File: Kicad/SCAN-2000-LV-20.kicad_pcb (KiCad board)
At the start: 2 copper layers, 220 x 67 mm, 151 parts, among them J1 FTDI, J10 OUTPUT-BUS-A, J11 OUTPUT-BUS-B, J12 Test, J13 Conn_02x04_Counter_Clockwise, J2 Conn_01x02, J3 Conn_01x02, J4 BUS-A-INPUT, J5 SWD, J6 BUS-A-INPUT, J7 BUS-B-INPUT, J8 BUS-B-INPUT, J9 MOLEX 85050-0000, K1 EC2-3TNU, U1 STM32G030, U10 DG412, U11 DG412, U12 RB-0515D, U13 MDC3105, U14 TPS78233DDC, U15 TL7733BD, U16 MDC3105, U17 RB-0505S, U2 DG412, U3 DG412, U4 DG412, U5 DG412, U6 DG412, U7 DG412, U8 DG412, U9 DG412

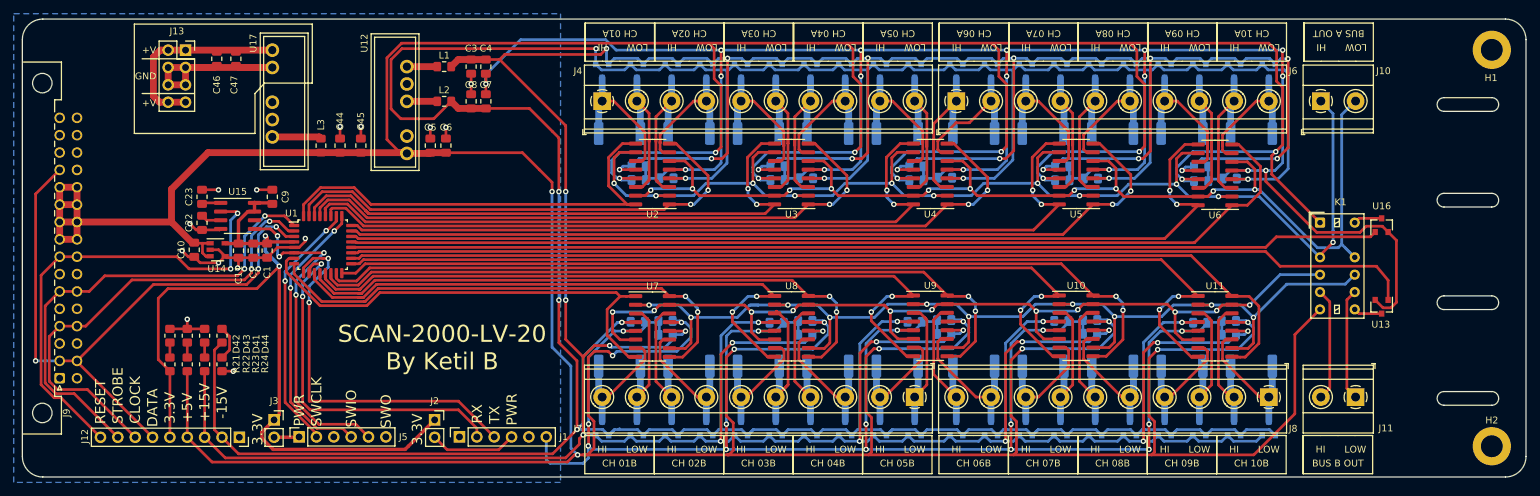
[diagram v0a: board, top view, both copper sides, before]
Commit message: Board layout for the Switches
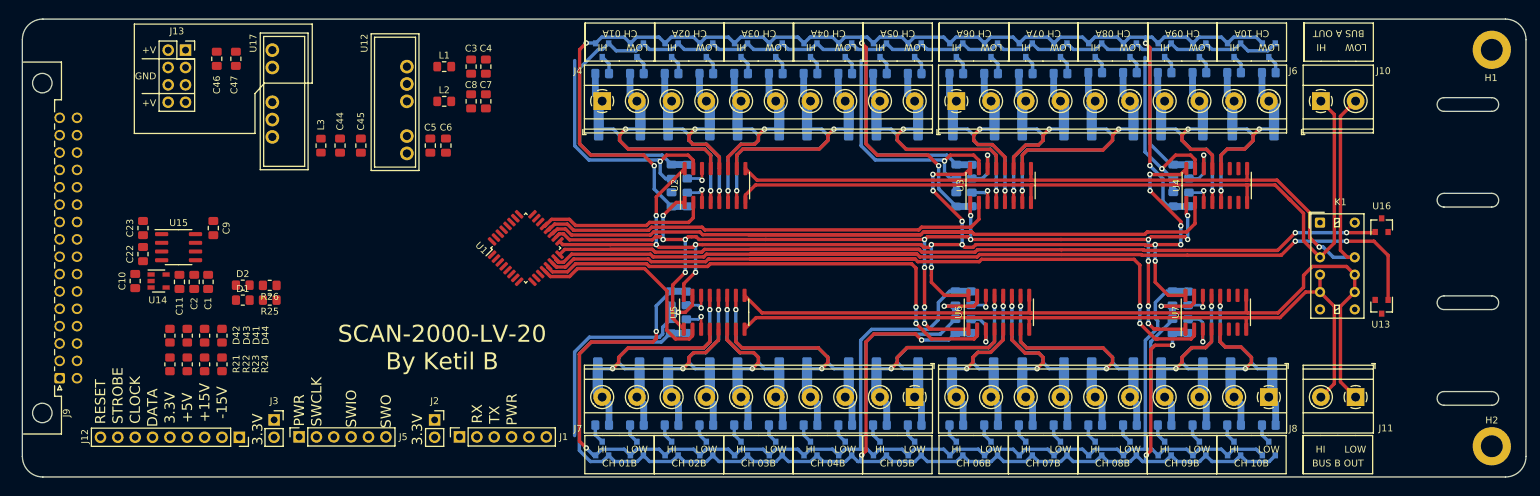
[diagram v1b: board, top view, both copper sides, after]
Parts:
- removed C13, C15, C17, C18, C19, C20, C21, C25, C27, C30, C32, C34, C35, C36, C37, C38, C40, C42: 0.1u, Capacitors-SMD:C_0805_2012Metric_Pad1.18x1.45mm_HandSolder
- removed U10, U11, U8, U9: DG412, SMD-SO:SOIC-16_3.9x9.9mm_P1.27mm
- added D45: BAV199, Package_TO_SOT_SMD:SOT-23, B.Cu at (185.3, 629.3)
- added D46: BAV199, Package_TO_SOT_SMD:SOT-23, B.Cu at (190.4, 629.3)
- added D47: BAV199, Package_TO_SOT_SMD:SOT-23, B.Cu at (195.5, 629.3)
- added D48: BAV199, Package_TO_SOT_SMD:SOT-23, B.Cu at (200.6, 629.3)
- added D49: BAV199, Package_TO_SOT_SMD:SOT-23, B.Cu at (206.7, 629.3)
- added D50: BAV199, Package_TO_SOT_SMD:SOT-23, B.Cu at (211.7, 629.3)
- added D51: BAV199, Package_TO_SOT_SMD:SOT-23, B.Cu at (216.8, 629.3)
- added D52: BAV199, Package_TO_SOT_SMD:SOT-23, B.Cu at (221.9, 629.3)
- added D53: BAV199, Package_TO_SOT_SMD:SOT-23, B.Cu at (227.0, 629.3)
- added D54: BAV199, Package_TO_SOT_SMD:SOT-23, B.Cu at (232.1, 629.3)
- added D55: BAV199, Package_TO_SOT_SMD:SOT-23, B.Cu at (237.1, 629.3)
- added D56: BAV199, Package_TO_SOT_SMD:SOT-23, B.Cu at (242.2, 629.3)
- added D57: BAV199, Package_TO_SOT_SMD:SOT-23, B.Cu at (247.3, 629.3)
- added D58: BAV199, Package_TO_SOT_SMD:SOT-23, B.Cu at (252.4, 629.3)
- added R100: 200R, Resistors-SMD:R_0805_2012Metric_Pad1.20x1.40mm_HandSolder, B.Cu at (221.9, 625.9)
- added R101: 200R, Resistors-SMD:R_0805_2012Metric_Pad1.20x1.40mm_HandSolder, B.Cu at (227.0, 625.9)
- added R102: 200R, Resistors-SMD:R_0805_2012Metric_Pad1.20x1.40mm_HandSolder, B.Cu at (232.1, 625.9)
- added R103: 200R, Resistors-SMD:R_0805_2012Metric_Pad1.20x1.40mm_HandSolder, B.Cu at (237.1, 625.9)
- added R104: 200R, Resistors-SMD:R_0805_2012Metric_Pad1.20x1.40mm_HandSolder, B.Cu at (242.2, 625.9)
- added R105: 200R, Resistors-SMD:R_0805_2012Metric_Pad1.20x1.40mm_HandSolder, B.Cu at (247.3, 625.9)
- added R106: 200R, Resistors-SMD:R_0805_2012Metric_Pad1.20x1.40mm_HandSolder, B.Cu at (252.4, 625.9)
- added R25: R, Resistors-SMD:R_0805_2012Metric_Pad1.20x1.40mm_HandSolder, F.Cu at (106.2, 607.6)
- added R26: R, Resistors-SMD:R_0805_2012Metric_Pad1.20x1.40mm_HandSolder, F.Cu at (106.2, 605.5)
- added R67: 200R, Resistors-SMD:R_0805_2012Metric_Pad1.20x1.40mm_HandSolder, B.Cu at (154.8, 574.5)
- added R68: 200R, Resistors-SMD:R_0805_2012Metric_Pad1.20x1.40mm_HandSolder, B.Cu at (159.9, 574.5)
- added R69: 200R, Resistors-SMD:R_0805_2012Metric_Pad1.20x1.40mm_HandSolder, B.Cu at (165.0, 574.5)
- added R70: 200R, Resistors-SMD:R_0805_2012Metric_Pad1.20x1.40mm_HandSolder, B.Cu at (170.1, 574.5)
- added R71: 200R, Resistors-SMD:R_0805_2012Metric_Pad1.20x1.40mm_HandSolder, B.Cu at (175.2, 574.5)
- added R72: 200R, Resistors-SMD:R_0805_2012Metric_Pad1.20x1.40mm_HandSolder, B.Cu at (180.2, 574.5)
- added R73: 200R, Resistors-SMD:R_0805_2012Metric_Pad1.20x1.40mm_HandSolder, B.Cu at (185.3, 574.5)
- added R74: 200R, Resistors-SMD:R_0805_2012Metric_Pad1.20x1.40mm_HandSolder, B.Cu at (190.4, 574.5)
- added R75: 200R, Resistors-SMD:R_0805_2012Metric_Pad1.20x1.40mm_HandSolder, B.Cu at (195.5, 574.5)
- added R76: 200R, Resistors-SMD:R_0805_2012Metric_Pad1.20x1.40mm_HandSolder, B.Cu at (200.6, 574.5)
- added R77: 200R, Resistors-SMD:R_0805_2012Metric_Pad1.20x1.40mm_HandSolder, B.Cu at (206.7, 574.5)
- added R78: 200R, Resistors-SMD:R_0805_2012Metric_Pad1.20x1.40mm_HandSolder, B.Cu at (211.7, 574.5)
- added R79: 200R, Resistors-SMD:R_0805_2012Metric_Pad1.20x1.40mm_HandSolder, B.Cu at (216.8, 574.5)
- added R80: 200R, Resistors-SMD:R_0805_2012Metric_Pad1.20x1.40mm_HandSolder, B.Cu at (221.9, 574.5)
- added R81: 200R, Resistors-SMD:R_0805_2012Metric_Pad1.20x1.40mm_HandSolder, B.Cu at (227.0, 574.3)
- added R82: 200R, Resistors-SMD:R_0805_2012Metric_Pad1.20x1.40mm_HandSolder, B.Cu at (232.1, 574.3)
- added R83: 200R, Resistors-SMD:R_0805_2012Metric_Pad1.20x1.40mm_HandSolder, B.Cu at (237.1, 574.3)
- added R84: 200R, Resistors-SMD:R_0805_2012Metric_Pad1.20x1.40mm_HandSolder, B.Cu at (242.2, 574.3)
- added R85: 200R, Resistors-SMD:R_0805_2012Metric_Pad1.20x1.40mm_HandSolder, B.Cu at (247.3, 574.3)
- added R86: 200R, Resistors-SMD:R_0805_2012Metric_Pad1.20x1.40mm_HandSolder, B.Cu at (252.4, 574.3)
- added R87: 200R, Resistors-SMD:R_0805_2012Metric_Pad1.20x1.40mm_HandSolder, B.Cu at (154.8, 625.9)
- added R88: 200R, Resistors-SMD:R_0805_2012Metric_Pad1.20x1.40mm_HandSolder, B.Cu at (159.9, 625.9)
- added R89: 200R, Resistors-SMD:R_0805_2012Metric_Pad1.20x1.40mm_HandSolder, B.Cu at (165.0, 625.9)
- added R90: 200R, Resistors-SMD:R_0805_2012Metric_Pad1.20x1.40mm_HandSolder, B.Cu at (170.1, 625.9)
- added R91: 200R, Resistors-SMD:R_0805_2012Metric_Pad1.20x1.40mm_HandSolder, B.Cu at (175.2, 625.9)
- added R92: 200R, Resistors-SMD:R_0805_2012Metric_Pad1.20x1.40mm_HandSolder, B.Cu at (180.2, 625.9)
- added R93: 200R, Resistors-SMD:R_0805_2012Metric_Pad1.20x1.40mm_HandSolder, B.Cu at (185.3, 625.9)
- added R94: 200R, Resistors-SMD:R_0805_2012Metric_Pad1.20x1.40mm_HandSolder, B.Cu at (190.4, 625.9)
- added R95: 200R, Resistors-SMD:R_0805_2012Metric_Pad1.20x1.40mm_HandSolder, B.Cu at (195.5, 625.9)
- added R96: 200R, Resistors-SMD:R_0805_2012Metric_Pad1.20x1.40mm_HandSolder, B.Cu at (200.6, 625.9)
- added R97: 200R, Resistors-SMD:R_0805_2012Metric_Pad1.20x1.40mm_HandSolder, B.Cu at (206.7, 625.9)
- added R98: 200R, Resistors-SMD:R_0805_2012Metric_Pad1.20x1.40mm_HandSolder, B.Cu at (211.7, 625.9)
- added R99: 200R, Resistors-SMD:R_0805_2012Metric_Pad1.20x1.40mm_HandSolder, B.Cu at (216.8, 625.9)
- D1, D2: value BAV199L -> LED; footprint SMD-SOT:SOT-23 -> Resistors-SMD:R_0805_2012Metric_Pad1.20x1.40mm_HandSolder; moved to F.Cu
- D10, D11, D12, D13, D14, D3, D4, D5, D6, D7, D8, D9: value BAV199L -> D; footprint SMD-SOT:SOT-23 -> Resistors-SMD:R_0805_2012Metric_Pad1.20x1.40mm_HandSolder
- D15, D16, D17, D18, D19, D20, D21, D22, D23, D24, D25, D26, D27, D28, D29, D30, D31, D32, D33, D34, D35, D36, D37, D38, D39, D40: value BAV199L -> BAV199; footprint SMD-SOT:SOT-23 -> Package_TO_SOT_SMD:SOT-23
- U2, U3, U4, U5, U6, U7: value DG412 -> DG409
- moved U7 82.4 mm to (244.6, 609.4), turned to 90 degrees
- moved D20 72.2 mm to (180.2, 571.0)
- moved D15 72.2 mm to (154.8, 571.0)
- moved D16 72.2 mm to (159.9, 571.0)
- moved D17 72.2 mm to (165.0, 571.0)
- moved D18 72.2 mm to (170.1, 571.0)
- moved D19 72.2 mm to (175.2, 571.0)
- moved D40 72.2 mm to (180.2, 629.3)
- moved D35 72.2 mm to (154.8, 629.3)
- moved D36 72.2 mm to (159.9, 629.3)
- moved D37 72.2 mm to (165.0, 629.3)
- moved D38 72.2 mm to (170.1, 629.3)
- moved D39 72.2 mm to (175.2, 629.3)
- moved D5 67.2 mm to (240.7, 588.8), turned to 90 degrees
- moved D2 65.6 mm to (102.2, 605.4), turned to 0 degrees
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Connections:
- D1 pad 1: -15V -> GND
- D1 pad 2: +15V -> Net-(D1-Pad2)
- D10 pad 1: -15V -> Net-(D10-Pad1)
- D11 pad 1: -15V -> Net-(D11-Pad1)
- D12 pad 2: +15V -> Net-(D12-Pad2)
- D13 pad 2: +15V -> Net-(D13-Pad2)
- D14 pad 2: +15V -> Net-(D14-Pad2)
- D15 pad 3: CHAN-08A-HI -> Net-(D15-Pad3)
- D16 pad 3: CHAN-08A-LO -> Net-(D16-Pad3)
- D17 pad 3: CHAN-09A-HI -> Net-(D17-Pad3)
- D18 pad 3: CHAN-09A-LO -> Net-(D18-Pad3)
- D19 pad 3: CHAN-10A-HI -> Net-(D19-Pad3)
- D2 pad 1: -15V -> GND
- D2 pad 2: +15V -> Net-(D2-Pad2)
- D20 pad 3: CHAN-10A-LO -> Net-(D20-Pad3)
- D21 pad 3: CHAN-01B-HI -> Net-(D21-Pad3)
- D22 pad 3: CHAN-01B-LO -> Net-(D22-Pad3)
- D23 pad 3: CHAN-02B-HI -> Net-(D23-Pad3)
- D24 pad 3: CHAN-02B-LO -> Net-(D24-Pad3)
- D25 pad 3: CHAN-03B-HI -> Net-(D25-Pad3)
- D26 pad 3: CHAN-03B-LO -> Net-(D26-Pad3)
- D27 pad 3: CHAN-04B-HI -> Net-(D27-Pad3)
- D28 pad 3: CHAN-04B-LO -> Net-(D28-Pad3)
- D29 pad 3: CHAN-05B-HI -> Net-(D29-Pad3)
- D3 pad 1: -15V -> Net-(D3-Pad1)
- D30 pad 3: CHAN-05B-LO -> Net-(D30-Pad3)
- D31 pad 3: CHAN-06B-HI -> Net-(D31-Pad3)
- D32 pad 3: CHAN-06B-LO -> Net-(D32-Pad3)
- D33 pad 3: CHAN-07B-HI -> Net-(D33-Pad3)
- D34 pad 3: CHAN-07B-LO -> Net-(D34-Pad3)
- D35 pad 3: CHAN-08B-HI -> Net-(D35-Pad3)
- D36 pad 3: CHAN-08B-LO -> Net-(D36-Pad3)
- D37 pad 3: CHAN-09B-HI -> Net-(D37-Pad3)
- D38 pad 3: CHAN-09B-LO -> Net-(D38-Pad3)
- D39 pad 3: CHAN-10B-HI -> Net-(D39-Pad3)
- D4 pad 1: -15V -> Net-(D4-Pad1)
- D40 pad 3: CHAN-10B-LO -> Net-(D40-Pad3)
- D5 pad 1: -15V -> Net-(D5-Pad1)
- D6 pad 2: +15V -> Net-(D6-Pad2)
- D7 pad 2: +15V -> Net-(D7-Pad2)
- D8 pad 2: +15V -> Net-(D8-Pad2)
- D9 pad 1: -15V -> Net-(D9-Pad1)
- J1 pad 1: DTR -> (no net)
- J1 pad 5: CTS -> (no net)
- J11 pad 1: Net-(J11-Pad1) -> BUS-B-LO
- J11 pad 2: Net-(J11-Pad2) -> BUS-B-HI
- J5 pad 6: SWO -> (no net)
- K1 pad 5: Net-(J11-Pad2) -> BUS-B-HI
- K1 pad 8: Net-(J11-Pad1) -> BUS-B-LO
- U1 pad 1: STROBE -> DATA
- U1 pad 11: CHAN-03B-CON -> (no net)
- U1 pad 12: CHAN-04B-CON -> EN-U5-DIG
- U1 pad 13: CHAN-05B-CON -> EN-U6-DIG
- U1 pad 14: CHAN-06B-CON -> EN-U7-Dig
- U1 pad 15: CHAN-07B-CON -> BUS-RESET
- U1 pad 16: CHAN-08B-CON -> BUS-SET
- U1 pad 17: CHAN-09B-CON -> CON-A1-DIG
- U1 pad 18: CHAN-10B-CON -> CON-A0-DIG
- U1 pad 19: BUS-RESET -> EN-U4-DIG
- U1 pad 2: CLOCK -> STROBE
- U1 pad 20: BUS-SET -> EN-U3-DIG
- U1 pad 21: CHAN-10A-CON -> EN-U2-DIG
- U1 pad 22: CHAN-09A-CON -> (no net)
- U1 pad 23: CHAN-08A-CON -> (no net)
- U1 pad 24: CHAN-07A-CON -> (no net)
- U1 pad 27: CHAN-06A-CON -> (no net)
- U1 pad 28: CHAN-05A-CON -> (no net)
- U1 pad 29: CHAN-04A-CON -> (no net)
- U1 pad 3: DATA -> CLOCK
- U1 pad 30: CHAN-03A-CON -> (no net)
- U1 pad 31: CHAN-02A-CON -> Net-(R26-Pad1)
- U1 pad 32: CHAN-01A-CON -> Net-(R25-Pad1)
- U1 pad 7: CHAN-01B-CON -> (no net)
- U1 pad 8: CHAN-02B-CON -> (no net)
- U15 pad 6: Net-(U15-Pad6) -> (no net)
- U17 pad 4: Net-(U17-Pad4) -> (no net)
- U2 pad 1: CHAN-02A-CON -> CON-A0-DIG
- U2 pad 10: BUS-A-HI -> CHAN-04A-LO
- U2 pad 11: CHAN-01A-HI -> CHAN-03A-LO
- U2 pad 12: +15V -> CHAN-02A-LO
- U2 pad 13: +5V -> CHAN-01A-LO
- U2 pad 14: CHAN-01A-LO -> Net-(D3-Pad1)
- U2 pad 15: BUS-A-LO -> GND
- U2 pad 16: CHAN-01A-CON -> CON-A1-DIG
- U2 pad 2: BUS-A-HI -> EN-U2-DIG
- U2 pad 3: CHAN-02A-HI -> Net-(D6-Pad2)
- U2 pad 4: -15V -> CHAN-01A-HI
- U2 pad 5: GND -> CHAN-02A-HI
- U2 pad 6: BUS-A-LO -> CHAN-03A-HI
- U2 pad 7: CHAN-02A-LO -> CHAN-04A-HI
- U2 pad 8: CHAN-02A-CON -> BUS-A-HI
- U2 pad 9: CHAN-01A-CON -> BUS-A-LO
- U3 pad 1: CHAN-04A-CON -> CON-A0-DIG
- U3 pad 10: BUS-A-HI -> CHAN-08A-LO
- U3 pad 11: CHAN-03A-HI -> CHAN-07A-LO
- U3 pad 12: +15V -> CHAN-06A-LO
- U3 pad 13: +5V -> CHAN-05A-LO
- U3 pad 14: CHAN-03A-LO -> Net-(D4-Pad1)
- U3 pad 15: BUS-A-LO -> GND
- U3 pad 16: CHAN-03A-CON -> CON-A1-DIG
- U3 pad 2: BUS-A-HI -> EN-U3-DIG
- U3 pad 3: CHAN-04A-HI -> Net-(D7-Pad2)
- U3 pad 4: -15V -> CHAN-05A-HI
- U3 pad 5: GND -> CHAN-06A-HI
- U3 pad 6: BUS-A-LO -> CHAN-07A-HI
- U3 pad 7: CHAN-04A-LO -> CHAN-08A-HI
- U3 pad 8: CHAN-04A-CON -> BUS-A-HI
- U3 pad 9: CHAN-03A-CON -> BUS-A-LO
- U4 pad 1: CHAN-06A-CON -> CON-A0-DIG
- U4 pad 10: BUS-A-HI -> (no net)
- U4 pad 11: CHAN-05A-HI -> (no net)
- U4 pad 12: +15V -> CHAN-10A-LO
- U4 pad 13: +5V -> CHAN-09A-LO
- U4 pad 14: CHAN-05A-LO -> Net-(D5-Pad1)
- U4 pad 15: BUS-A-LO -> GND
- U4 pad 16: CHAN-05A-CON -> CON-A1-DIG
- U4 pad 2: BUS-A-HI -> EN-U4-DIG
- U4 pad 3: CHAN-06A-HI -> Net-(D8-Pad2)
- U4 pad 4: -15V -> CHAN-09A-HI
- U4 pad 5: GND -> CHAN-10A-HI
- U4 pad 6: BUS-A-LO -> (no net)
- U4 pad 7: CHAN-06A-LO -> (no net)
- U4 pad 8: CHAN-06A-CON -> BUS-A-HI
- U4 pad 9: CHAN-05A-CON -> BUS-A-LO
- U5 pad 1: CHAN-08A-CON -> CON-A0-DIG
- U5 pad 10: BUS-A-HI -> CHAN-04B-LO
- U5 pad 11: CHAN-07A-HI -> CHAN-03B-LO
- U5 pad 12: +15V -> CHAN-02B-LO
- U5 pad 13: +5V -> CHAN-01B-LO
- U5 pad 14: CHAN-07A-LO -> Net-(D9-Pad1)
- U5 pad 15: BUS-A-LO -> GND
- U5 pad 16: CHAN-07A-CON -> CON-A1-DIG
- U5 pad 2: BUS-A-HI -> EN-U5-DIG
- U5 pad 3: CHAN-08A-HI -> Net-(D12-Pad2)
- U5 pad 4: -15V -> CHAN-01B-HI
- U5 pad 5: GND -> CHAN-02B-HI
- U5 pad 6: BUS-A-LO -> CHAN-03B-HI
- U5 pad 7: CHAN-08A-LO -> CHAN-04B-HI
- U5 pad 8: CHAN-08A-CON -> BUS-B-HI
- U5 pad 9: CHAN-07A-CON -> BUS-B-LO
- U6 pad 1: CHAN-10A-CON -> CON-A0-DIG
- U6 pad 10: BUS-A-HI -> CHAN-08B-LO
- U6 pad 11: CHAN-09A-HI -> CHAN-07B-LO
- U6 pad 12: +15V -> CHAN-06B-LO
- U6 pad 13: +5V -> CHAN-05B-LO
- U6 pad 14: CHAN-09A-LO -> Net-(D11-Pad1)
- U6 pad 15: BUS-A-LO -> GND
- U6 pad 16: CHAN-09A-CON -> CON-A1-DIG
- U6 pad 2: BUS-A-HI -> EN-U6-DIG
- U6 pad 3: CHAN-10A-HI -> Net-(D14-Pad2)
- U6 pad 4: -15V -> CHAN-05B-HI
- U6 pad 5: GND -> CHAN-06B-HI
- U6 pad 6: BUS-A-LO -> CHAN-07B-HI
- U6 pad 7: CHAN-10A-LO -> CHAN-08B-HI
- U6 pad 8: CHAN-10A-CON -> BUS-B-HI
- U6 pad 9: CHAN-09A-CON -> BUS-B-LO
- U7 pad 1: CHAN-01B-CON -> CON-A0-DIG
- U7 pad 10: BUS-B-LO -> (no net)
- U7 pad 11: CHAN-02B-LO -> (no net)
- U7 pad 12: +15V -> CHAN-10B-LO
- U7 pad 13: +5V -> CHAN-09B-LO
- U7 pad 14: CHAN-02B-HI -> Net-(D10-Pad1)
- U7 pad 15: BUS-B-HI -> GND
- U7 pad 16: CHAN-02B-CON -> CON-A1-DIG
- U7 pad 2: BUS-B-LO -> EN-U7-Dig
- U7 pad 3: CHAN-01B-LO -> Net-(D13-Pad2)
- U7 pad 4: -15V -> CHAN-09B-HI
- U7 pad 5: GND -> CHAN-10B-HI
- U7 pad 6: BUS-B-HI -> (no net)
- U7 pad 7: CHAN-01B-HI -> (no net)
- U7 pad 8: CHAN-01B-CON -> BUS-B-HI
- U7 pad 9: CHAN-02B-CON -> BUS-B-LO
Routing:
- net +5V: track 895.9 -> 0.00 mm, vias 22 -> 0
- net GND: track 631.7 -> 204.1 mm, vias 46 -> 6
- net +15V: track 692.5 -> 412.7 mm, vias 33 -> 2
- net -15V: track 660.3 -> 422.9 mm, vias 14 -> 10
- net CON-A1-DIG: track 0.00 -> 171.4 mm, vias 0 -> 16
- net CON-A0-DIG: track 0.00 -> 164.7 mm, vias 0 -> 16
- net CHAN-10B-CON: track 146.3 -> 0.00 mm
- net CHAN-10A-CON: track 145.4 -> 0.00 mm
- net CHAN-09B-CON: track 142.7 -> 0.00 mm, vias 2 -> 0
- net CHAN-09A-CON: track 141.3 -> 0.00 mm, vias 2 -> 0
- net EN-U4-DIG: track 0.00 -> 131.2 mm
- net EN-U7-Dig: track 0.00 -> 130.5 mm, vias 0 -> 2
- net CHAN-08B-CON: track 128.0 -> 0.00 mm, vias 2 -> 0
- net CHAN-08A-CON: track 126.7 -> 0.00 mm, vias 2 -> 0
- net CHAN-07B-CON: track 125.3 -> 0.00 mm, vias 2 -> 0
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- removed copper zone on B.Cu, net GND
